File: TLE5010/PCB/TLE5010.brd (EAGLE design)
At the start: 155 x 154.5 mm, 8 parts

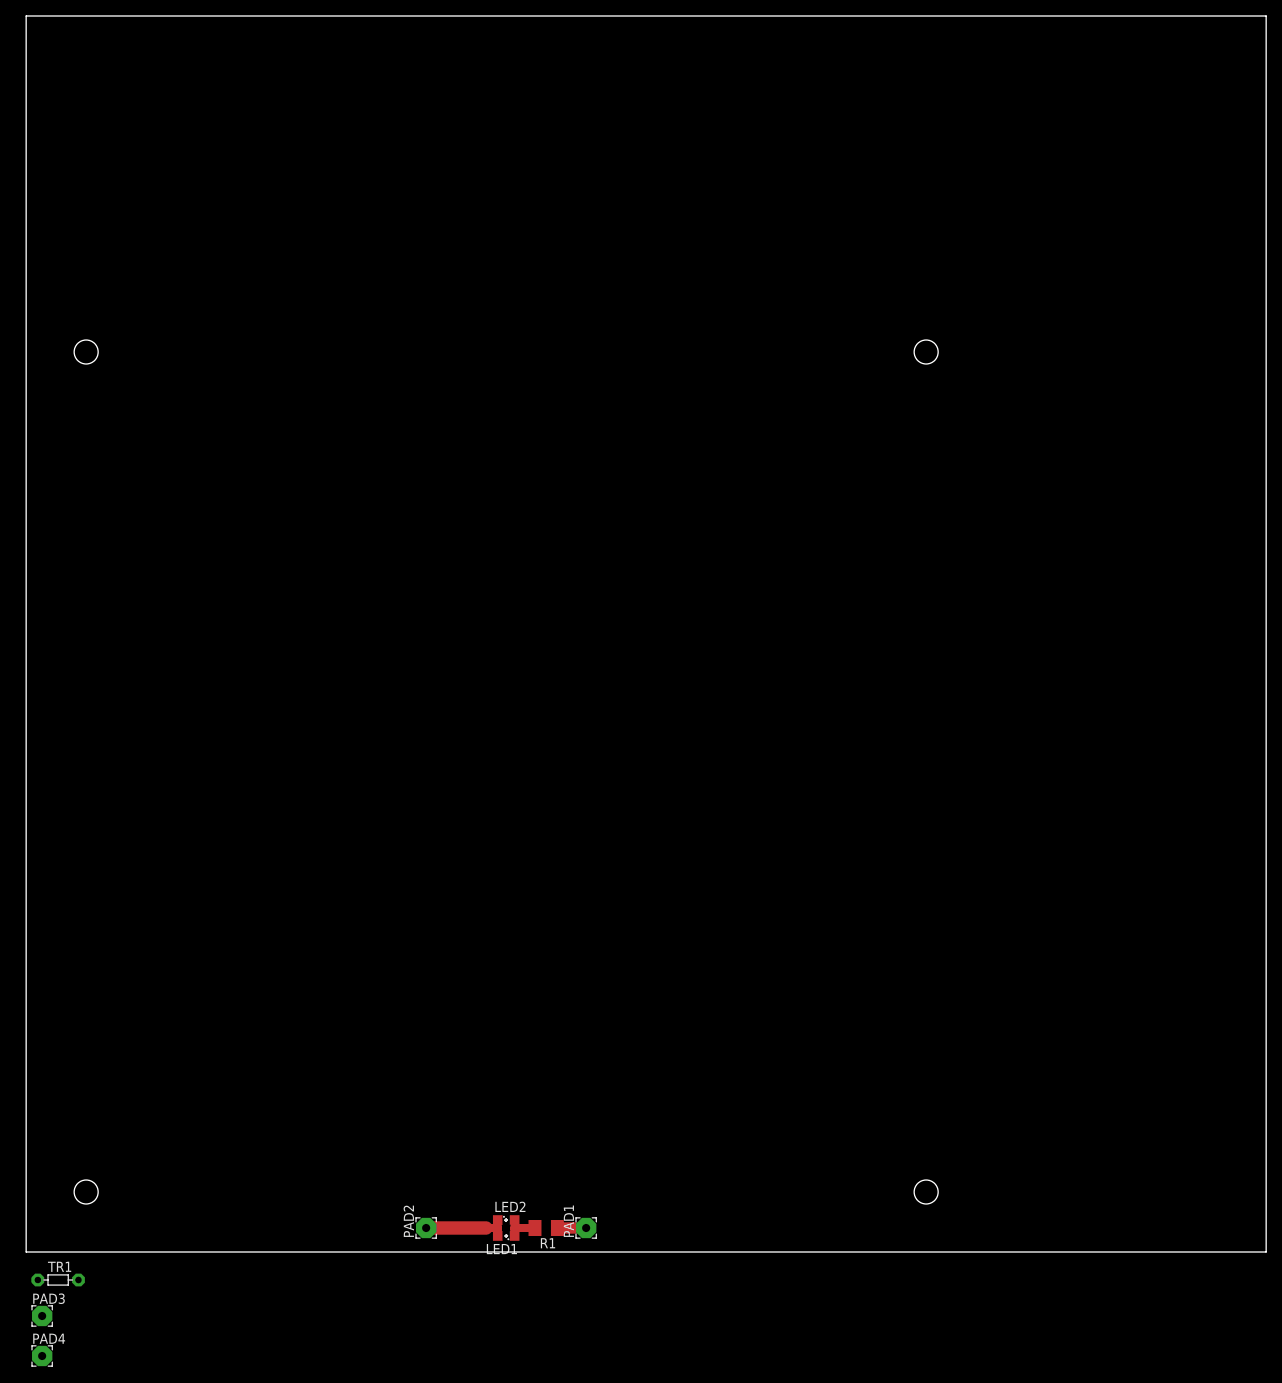
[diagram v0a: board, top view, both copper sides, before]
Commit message: TLE5010 added, folders cleanup
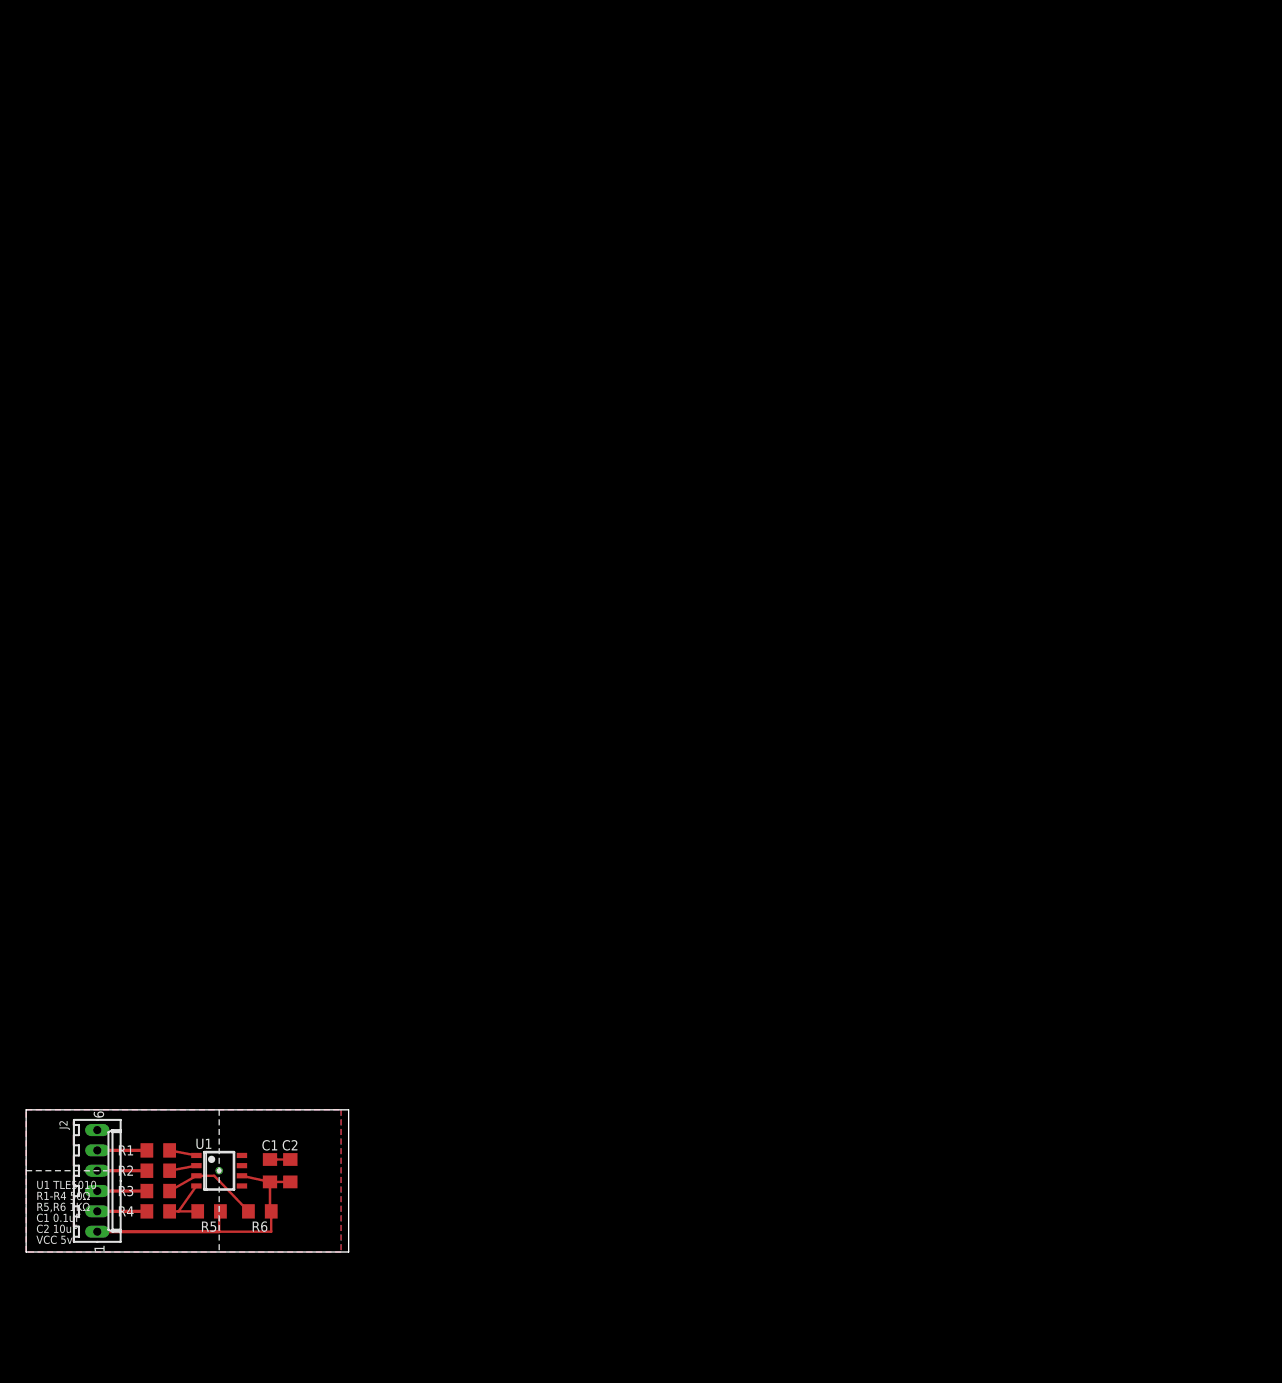
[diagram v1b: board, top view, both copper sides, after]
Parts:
- removed LED1, LED2: (no value), led:SML0805
- removed PAD1, PAD2, PAD3, PAD4: (no value), wirepad:2,54/1,0
- removed TR1: (no value), discrete:R-5
- added C1: 0.1uF, resistor:C1206
- added C2: 10uF, resistor:C1206
- added J2: 22-27-2061-06, con-molex:6410-06
- added R2, R3, R4: 50, resistor:R1206
- added R5, R6: 1K, resistor:R1206
- added U1: TLE5010, infineon:PG-DSO-8
- R1: value (none) -> 50; device rcl:M1206 -> resistor:R1206
- moved R1 49.5 mm to (16.5, 12.7), turned to 0 degrees
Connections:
- removed net N$4: LED1.C, LED2.A, R1.2
- new net CLK: J2.5, R1.1
- new net CS: J2.3, R3.1
- new net DATA: R4.2, R5.1, U1.4
- new net GND: C1.1, C2.1, J2.6, U1.5, U1.7, U1.8
- new net MISO: J2.2, R4.1
- new net SCK: J2.4, R2.1
- new net VCC: C1.2, C2.2, J2.1, R5.2, R6.2, U1.6
- net N$1: now also R1.2, U1.1; no longer LED1.A, LED2.C, PAD1.1, PAD2.1, R1.1
- net N$2: now also R2.2, U1.2; no longer PAD3.1, TR1.2
- net N$3: now also R3.2, R6.1, U1.3; no longer PAD4.1, TR1.1
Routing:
- net VCC: track 0.00 -> 36.8 mm
- net N$3: track 0.00 -> 12.2 mm
- net N$1: track 15.5 -> 3.41 mm
- net DATA: track 0.00 -> 7.61 mm
- net SCK: track 0.00 -> 6.20 mm
- net MISO: track 0.00 -> 6.20 mm
- net CS: track 0.00 -> 6.20 mm
- net CLK: track 0.00 -> 6.20 mm
- net N$4: track 5.55 -> 0.00 mm
- net N$2: track 0.00 -> 3.41 mm
- net GND: track 0.00 -> 2.57 mm, vias 0 -> 1
- added copper zone on layer 1, net GND
- added copper zone on layer 16, net GND
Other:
- board size 155 x 154.5 mm -> 40.3 x 17.8 mm
- board text added: "CLK"
- board text added: "CS"
- board text added: "Gnd"
- board text added: "MISO"
- board text added: "SCK"
- board text added: "U1 TLE5010 R1-R4 50Ω R5,R6 1KΩ C1 0.1uF C2 10uF VCC 5v"
- board text added: "Vcc"
- board text removed: "12V 40W"
- board text removed: "3.6R"

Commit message: TLE5010.brd fixed
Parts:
- J2: value 22-27-2061-06 -> 22-05-7068-06; device con-molex:6410-06 -> con-molex:7395-06
- moved J2 7.01 mm to (15.9, 9.53), turned to 90 degrees
- moved R5 6.35 mm to (29.2, 5.08)
- moved R6 6.35 mm to (35.6, 5.08)
- moved U1 6.35 mm to (30.5, 10.2)
- moved C1 6.35 mm to (36.8, 10.2)
- moved R1 6.35 mm to (22.9, 12.7)
- moved R2 6.35 mm to (22.9, 10.2)
- moved R3 6.35 mm to (22.9, 7.62)
- moved R4 6.35 mm to (22.9, 5.08)
- moved C2 6.35 mm to (39.4, 10.2)
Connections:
- net CLK: now also J2.2; no longer J2.5
- net CS: now also J2.4; no longer J2.3
- net GND: now also J2.1; no longer J2.6
- net MISO: now also J2.5; no longer J2.2
- net SCK: now also J2.3; no longer J2.4
- net VCC: now also J2.6; no longer J2.1
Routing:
- net VCC: track 36.8 -> 34.5 mm
- net DATA: track 7.61 -> 6.74 mm
- removed copper zone on layer 16, net GND
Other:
- board size 40.3 x 17.8 mm -> 60 x 20 mm
